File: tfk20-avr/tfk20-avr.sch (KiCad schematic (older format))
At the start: 31 parts, among them J1 USB_C_Receptacle_USB2.0, J2 AVR-ISP-6, SW1 Reset, U1 ATmega32U4-AU, Y1 16MHz

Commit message: Continue routing
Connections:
- net COL_0: now also U1.29 (PB5); no longer U1.28 (PB4)
- net COL_1: now also U1.28 (PB4); no longer U1.29 (PB5)
- net COL_2: now also U1.27 (PD7); no longer U1.30 (PB6)
- net COL_3: now also U1.30 (PB6); no longer U1.27 (PD7)
- net ROW_0: now also U1.36 (PF7); no longer U1.41 (PF0)
- net ROW_1: now also U1.37 (PF6); no longer U1.40 (PF1)
- net ROW_2: now also U1.38 (PF5); no longer U1.39 (PF4)
- net ROW_3: now also U1.39 (PF4); no longer U1.38 (PF5)
- net ROW_4: now also U1.40 (PF1); no longer U1.37 (PF6)
- net ROW_5: now also U1.41 (PF0); no longer U1.36 (PF7)
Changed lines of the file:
@@
 Wire Wire Line
 	10150 5550 10050 5550
-Text Label 10150 5150 0    50   ~ 0
+Text Label 10150 5650 0    50   ~ 0
 ROW_0
+Text Label 10150 5550 0    50   ~ 0
+ROW_1
+Text Label 10150 5450 0    50   ~ 0
+ROW_2
 Text Label 10150 5250 0    50   ~ 0
-ROW_1
-Text Label 10150 5350 0    50   ~ 0
-ROW_2
-Text Label 10150 5550 0    50   ~ 0
 ROW_4
 Wire Wire Line
 	10050 5650 10150 5650
-Text Label 10150 5650 0    50   ~ 0
+Text Label 10150 5150 0    50   ~ 0
 ROW_5
-Text Label 10150 5450 0    50   ~ 0
+Text Label 10150 5350 0    50   ~ 0
 ROW_3
 Wire Wire Line
 	10050 5450 10150 5450
+Text Label 10150 3250 0    50   ~ 0
+COL_0
 Text Label 10150 3150 0    50   ~ 0
-COL_0
-Text Label 10150 3250 0    50   ~ 0
 COL_1
+Text Label 10150 4650 0    50   ~ 0
+COL_2
 Text Label 10150 3350 0    50   ~ 0
-COL_2
-Text Label 10150 4650 0    50   ~ 0
 COL_3
 Wire Wire Line

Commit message: Continue routing
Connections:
- net ROW_4: now also U1.41 (PF0); no longer U1.40 (PF1)
- net ROW_5: now also U1.40 (PF1); no longer U1.41 (PF0)
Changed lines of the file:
@@
 Text Label 10150 5450 0    50   ~ 0
 ROW_2
-Text Label 10150 5250 0    50   ~ 0
+Text Label 10150 5150 0    50   ~ 0
 ROW_4
 Wire Wire Line
 	10050 5650 10150 5650
-Text Label 10150 5150 0    50   ~ 0
+Text Label 10150 5250 0    50   ~ 0
 ROW_5
 Text Label 10150 5350 0    50   ~ 0

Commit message: Continue routing
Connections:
- net COL_0: now also U1.31 (PC6); no longer U1.29 (PB5)
- net COL_1: now also U1.29 (PB5); no longer U1.28 (PB4)
- net COL_2: now also U1.28 (PB4); no longer U1.27 (PD7)
- net COL_3: now also U1.27 (PD7); no longer U1.30 (PB6)
- net RGB_LIGHT: now also U1.30 (PB6); no longer U1.31 (PC6)
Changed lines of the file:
@@
 Wire Wire Line
 	10050 5450 10150 5450
+Text Label 10150 3650 0    50   ~ 0
+COL_0
 Text Label 10150 3250 0    50   ~ 0
-COL_0
+COL_1
 Text Label 10150 3150 0    50   ~ 0
-COL_1
+COL_2
 Text Label 10150 4650 0    50   ~ 0
-COL_2
-Text Label 10150 3350 0    50   ~ 0
 COL_3
 Wire Wire Line
@@
 NoConn ~ 10100 4550
 NoConn ~ 10100 4950
-Text Label 10150 3650 0    50   ~ 0
+Text Label 10150 3350 0    50   ~ 0
 RGB_LIGHT
 Wire Wire Line

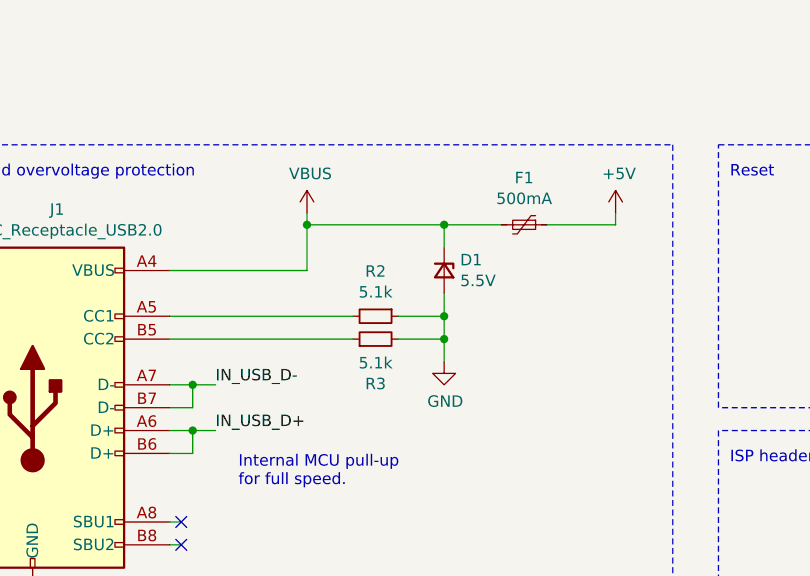
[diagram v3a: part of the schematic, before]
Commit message: Place OVP diode after fuse
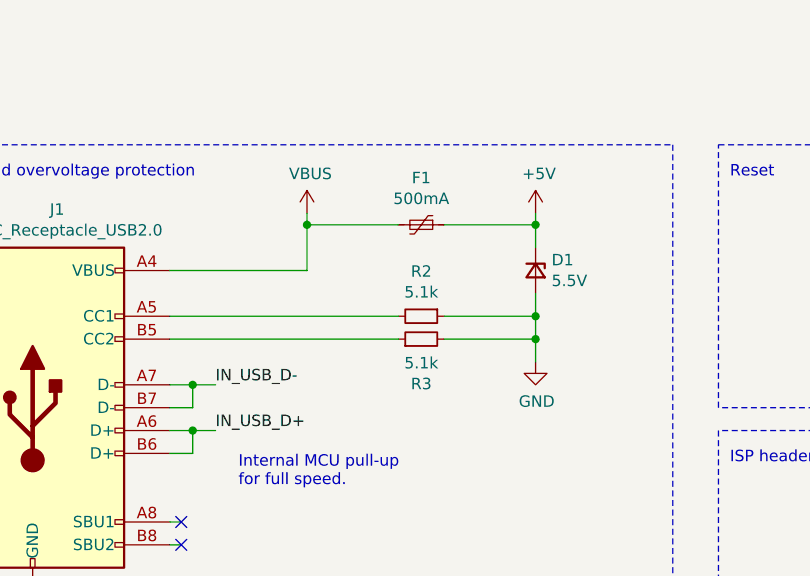
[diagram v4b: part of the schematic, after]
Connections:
- net +5V: now also D1.1 (K)
- net VBUS: no longer D1.1 (K)
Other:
- moved on the sheet: D1, F1, R2, R3
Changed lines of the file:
@@
 Shunt ESD away from \nGND and ICs to USB \nshield.
 Wire Wire Line
-	4350 1050 4350 1000
+	4000 1050 4000 1000
 $Comp
 L power:PWR_FLAG #FLG02
@@
 L power:+5V #PWR04
 U 1 1 60C2578C
-P 4350 1000
+P 4000 1000
 AR Path="/60C2578C" Ref="#PWR04"  Part="1"
 AR Path="/60815FFC/60C2578C" Ref="#PWR?"  Part="1"
-F 0 "#PWR04" H 4350 850 50  0001 C CNN
-F 1 "+5V" H 4365 1173 50  0000 C CNN
-F 2 "" H 4350 1000 50  0001 C CNN
-F 3 "" H 4350 1000 50  0001 C CNN
-	1    4350 1000
+F 0 "#PWR04" H 4000 850 50  0001 C CNN
+F 1 "+5V" H 4015 1173 50  0000 C CNN
+F 2 "" H 4000 1000 50  0001 C CNN
+F 3 "" H 4000 1000 50  0001 C CNN
+	1    4000 1000
 	1    0    0    -1
 $EndComp
@@
 L Device:Polyfuse_Small F1
 U 1 1 60C25792
-P 3950 1050
+P 3500 1050
 AR Path="/60C25792" Ref="F1"  Part="1"
 AR Path="/60815FFC/60C25792" Ref="F?"  Part="1"
-F 0 "F1" V 3745 1050 50  0000 C CNN
-F 1 "500mA" V 3836 1050 50  0000 C CNN
-F 2 "Fuse:Fuse_1206_3216Metric_Pad1.42x1.75mm_HandSolder" H 4000 850 50  0001 L CNN
-F 3 "~" H 3950 1050 50  0001 C CNN
-	1    3950 1050
+F 0 "F1" V 3295 1050 50  0000 C CNN
+F 1 "500mA" V 3386 1050 50  0000 C CNN
+F 2 "Fuse:Fuse_1206_3216Metric_Pad1.42x1.75mm_HandSolder" H 3550 850 50  0001 L CNN
+F 3 "~" H 3500 1050 50  0001 C CNN
+	1    3500 1050
 	0    1    1    0
 $EndComp
@@
 L Device:R_Small R2
 U 1 1 60C257CE
-P 3300 1450
+P 3500 1450
 AR Path="/60C257CE" Ref="R2"  Part="1"
 AR Path="/60815FFC/60C257CE" Ref="R?"  Part="1"
-F 0 "R2" V 3104 1450 50  0000 C CNN
-F 1 "5.1k" V 3195 1450 50  0000 C CNN
-F 2 "Resistor_SMD:R_0805_2012Metric_Pad1.20x1.40mm_HandSolder" H 3300 1450 50  0001 C CNN
-F 3 "~" H 3300 1450 50  0001 C CNN
-	1    3300 1450
+F 0 "R2" V 3304 1450 50  0000 C CNN
+F 1 "5.1k" V 3395 1450 50  0000 C CNN
+F 2 "Resistor_SMD:R_0805_2012Metric_Pad1.20x1.40mm_HandSolder" H 3500 1450 50  0001 C CNN
+F 3 "~" H 3500 1450 50  0001 C CNN
+	1    3500 1450
 	0    1    1    0
 $EndComp
@@
 L Device:R_Small R3
 U 1 1 60C257D4
-P 3300 1550
+P 3500 1550
 AR Path="/60C257D4" Ref="R3"  Part="1"
 AR Path="/60815FFC/60C257D4" Ref="R?"  Part="1"
-F 0 "R3" V 3104 1550 50  0000 C CNN
-F 1 "5.1k" V 3195 1550 50  0000 C CNN
-F 2 "Resistor_SMD:R_0805_2012Metric_Pad1.20x1.40mm_HandSolder" H 3300 1550 50  0001 C CNN
-F 3 "~" H 3300 1550 50  0001 C CNN
-	1    3300 1550
+F 0 "R3" V 3304 1550 50  0000 C CNN
+F 1 "5.1k" V 3395 1550 50  0000 C CNN
+F 2 "Resistor_SMD:R_0805_2012Metric_Pad1.20x1.40mm_HandSolder" H 3500 1550 50  0001 C CNN
+F 3 "~" H 3500 1550 50  0001 C CNN
+	1    3500 1550
 	0    -1   -1   0
 $EndComp
 Wire Wire Line
-	3400 1450 3600 1450
-Wire Wire Line
-	3600 1450 3600 1550
-Wire Wire Line
-	3600 1550 3400 1550
-Wire Wire Line
-	3600 1650 3600 1550
-Connection ~ 3600 1550
+	3600 1450 4000 1450
+Wire Wire Line
+	4000 1450 4000 1550
+Wire Wire Line
+	4000 1550 3600 1550
+Wire Wire Line
+	4000 1650 4000 1550
+Connection ~ 4000 1550
 $Comp
 L power:GND #PWR09
 U 1 1 60C257E1
-P 3600 1650
+P 4000 1650
 AR Path="/60C257E1" Ref="#PWR09"  Part="1"
 AR Path="/60815FFC/60C257E1" Ref="#PWR?"  Part="1"
-F 0 "#PWR09" H 3600 1400 50  0001 C CNN
-F 1 "GND" H 3605 1477 50  0000 C CNN
-F 2 "" H 3600 1650 50  0001 C CNN
-F 3 "" H 3600 1650 50  0001 C CNN
-	1    3600 1650
-	1    0    0    -1
-$EndComp
-Wire Wire Line
-	4050 1050 4350 1050
-Wire Wire Line
-	2400 1450 3200 1450
-Wire Wire Line
-	2400 1550 3200 1550
+F 0 "#PWR09" H 4000 1400 50  0001 C CNN
+F 1 "GND" H 4005 1477 50  0000 C CNN
+F 2 "" H 4000 1650 50  0001 C CNN
+F 3 "" H 4000 1650 50  0001 C CNN
+	1    4000 1650
+	1    0    0    -1
+$EndComp
+Wire Wire Line
+	3600 1050 4000 1050
+Wire Wire Line
+	2400 1450 3400 1450
+Wire Wire Line
+	2400 1550 3400 1550
 Wire Notes Line
 	700  3800 2650 3800
@@
 	5150 7250 5150 7350
 Connection ~ 5150 7250
-Connection ~ 3600 1450
-Wire Wire Line
-	3000 1050 3600 1050
-Wire Wire Line
-	3600 1050 3850 1050
-Connection ~ 3600 1050
-Wire Wire Line
-	3600 1350 3600 1450
-Wire Wire Line
-	3600 1150 3600 1050
 $Comp
 L Device:D_Zener_Small D1
 U 1 1 60BED50D
-P 3600 1250
-F 0 "D1" V 3554 1320 50  0000 L CNN
-F 1 "5.5V" V 3645 1320 50  0000 L CNN
-F 2 "Diode_SMD:D_SOD-123" V 3600 1250 50  0001 C CNN
-F 3 "~" V 3600 1250 50  0001 C CNN
-	1    3600 1250
+P 4000 1250
+F 0 "D1" V 3954 1320 50  0000 L CNN
+F 1 "5.5V" V 4045 1320 50  0000 L CNN
+F 2 "Diode_SMD:D_SOD-123" V 4000 1250 50  0001 C CNN
+F 3 "~" V 4000 1250 50  0001 C CNN
+	1    4000 1250
 	0    1    1    0
 $EndComp
+Wire Wire Line
+	3000 1050 3400 1050
+Wire Wire Line
+	4000 1050 4000 1150
+Connection ~ 4000 1050
+Wire Wire Line
+	4000 1350 4000 1450
+Connection ~ 4000 1450
 $EndSCHEMATC
